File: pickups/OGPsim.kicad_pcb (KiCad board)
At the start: 2 copper layers, 8.3 x 10 mm, 9 parts, among them J1 Conn_01x03, J2 Conn_01x03, J3 Conn_01x02_MountingPin, Q3 QSB363, Q4 QSB363

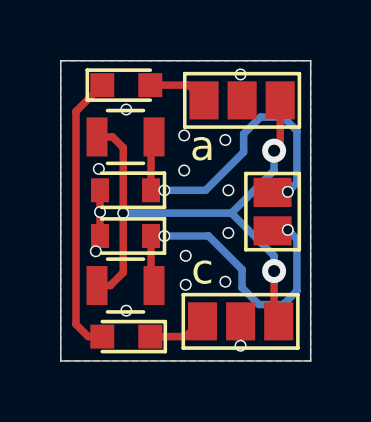
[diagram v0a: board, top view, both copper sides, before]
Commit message: Added name and date to silkscreen on all boards. Sending design to PCB fab house tonight!
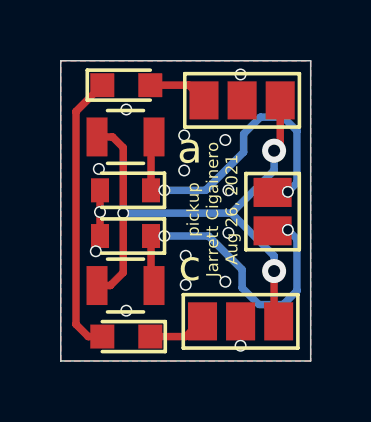
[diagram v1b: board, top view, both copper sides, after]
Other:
- board text added: "pickup Jarrett Cigainero Aug 26, 2021"
